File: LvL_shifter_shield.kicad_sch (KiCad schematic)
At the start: 11 parts, among them J1 Power, J2 Conn_02x08_Counter_Clockwise, J3 Conn_01x15_Socket, J4 Conn_01x15_Socket, U1 TXB0108DQSR, U2 TXB0108DQSR

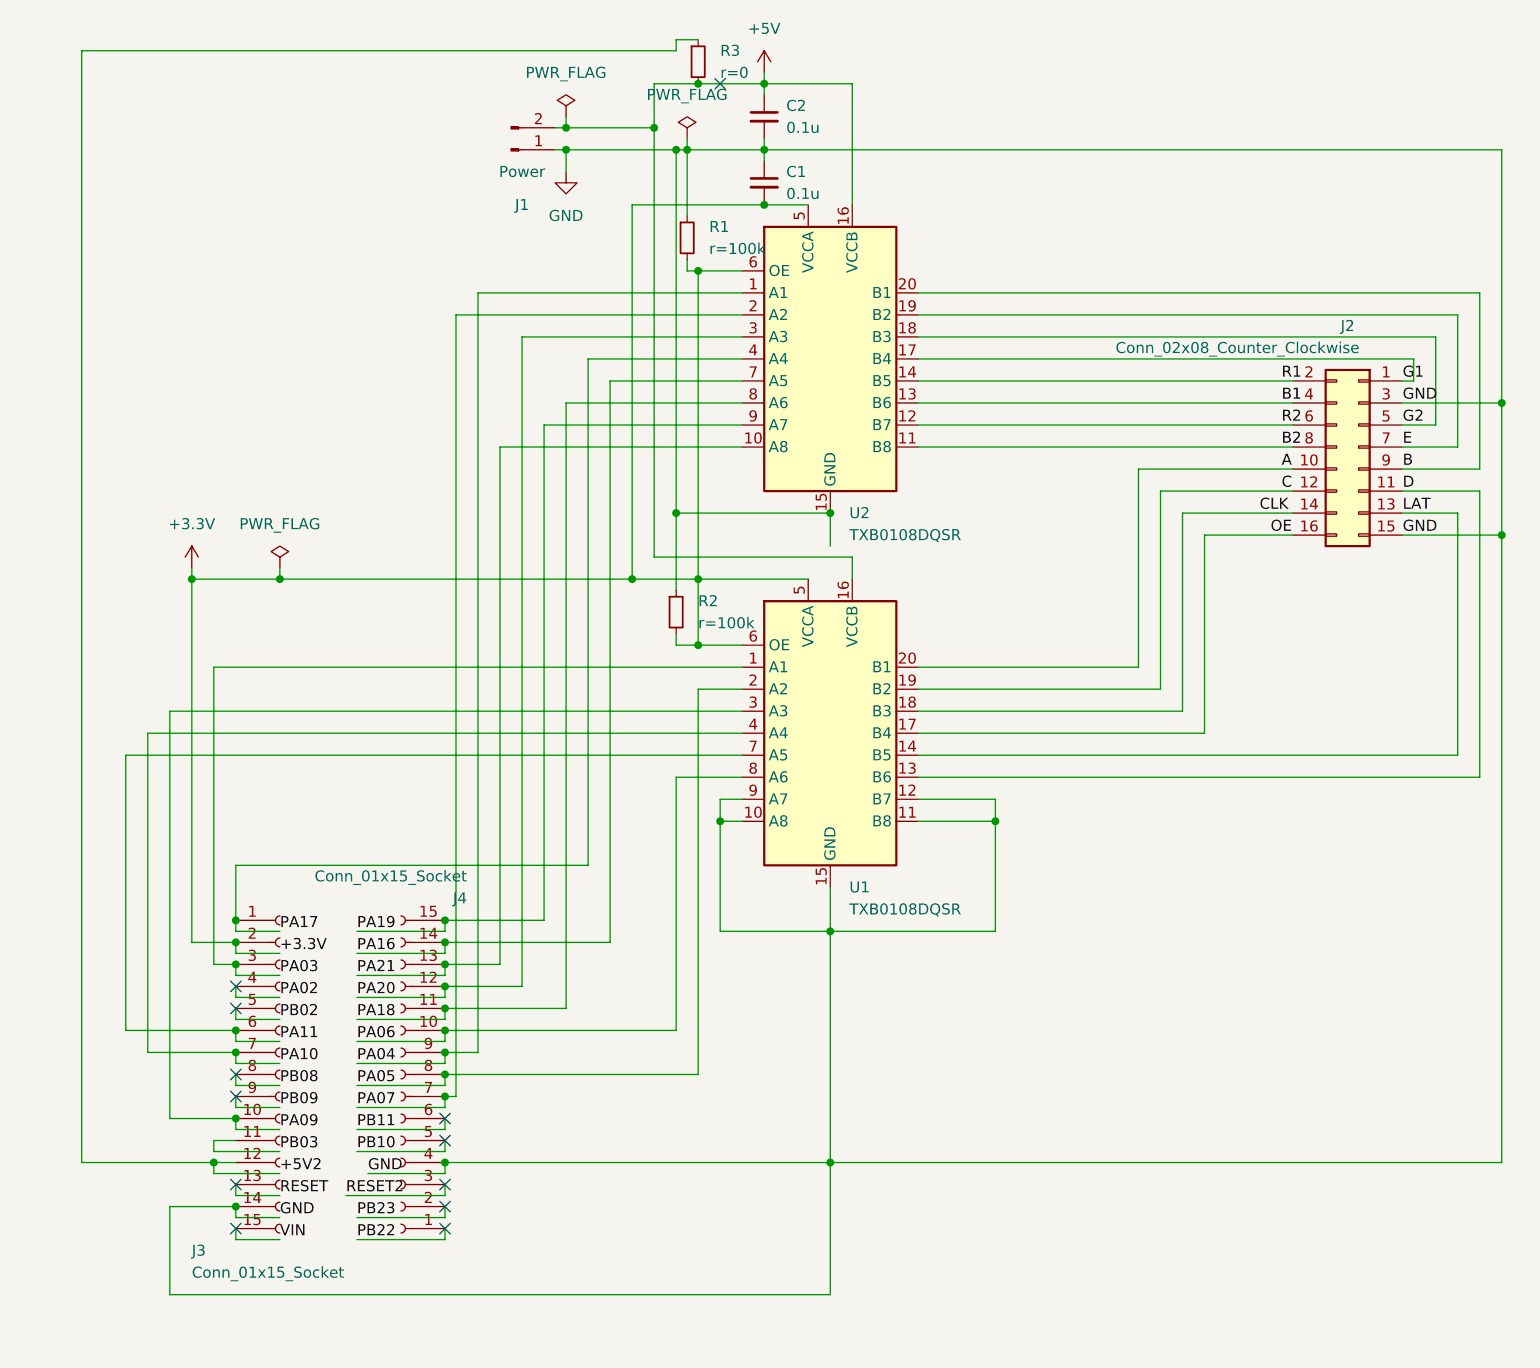
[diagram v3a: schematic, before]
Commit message: switched pin PA03 and PA02, added internal 5V
the dip switch can be used to get external 5v, internal or when none is selected the usb 5v from the arduino
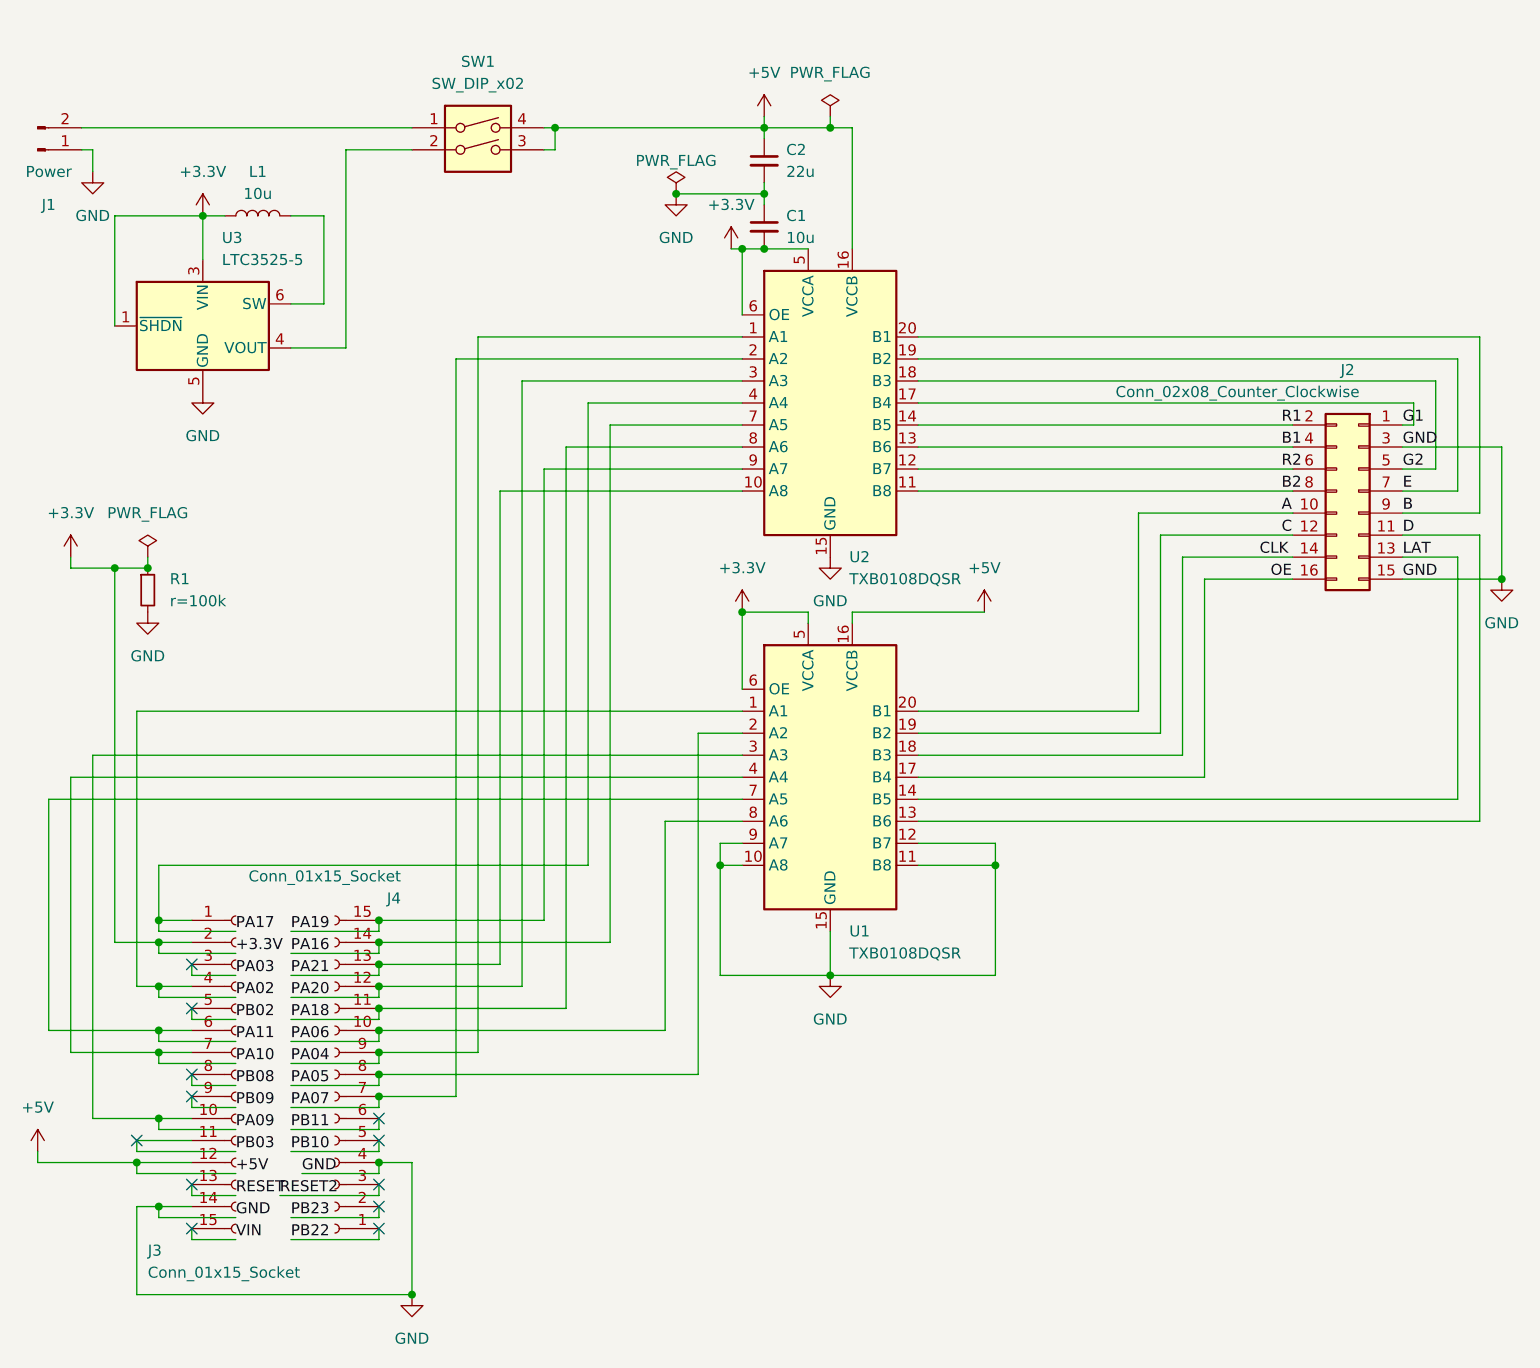
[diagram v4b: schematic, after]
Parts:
- removed R2: r=100k, Resistor_SMD:R_1206_3216Metric_Pad1.30x1.75mm_HandSolder, symbol Device:R_Small
- removed R3: r=0, Resistor_SMD:R_0603_1608Metric_Pad0.98x0.95mm_HandSolder, symbol Device:R_Small
- added L1: 10u, Inductor_SMD:L_1008_2520Metric_Pad1.43x2.20mm_HandSolder, symbol Device:L
- added SW1: SW_DIP_x02, Button_Switch_SMD:SW_DIP_SPSTx02_Slide_Copal_CHS-02A_W5.08mm_P1.27mm_JPin, symbol Switch:SW_DIP_x02
- added U3: LTC3525-5, Package_TO_SOT_SMD:SOT-363_SC-70-6, symbol Regulator_Switching:LTC3525-5
- C1: value 0.1u -> 10u
- C2: value 0.1u -> 22u
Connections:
- net +5V2 is gone; now on net +5V: J3.12 (Pin_12)
- net +3.3V: now also R1.1, L1.1, U3.1 (~{SHDN}), U3.3 (VIN); no longer R1.2
- net +5V: now also SW1.3, SW1.4; no longer J1.2 (Pin_2)
- net GND: now also R1.2, U3.2 (GND), U3.5 (GND); no longer R1.1
- net PA02: now also U1.1 (A1)
- net PA03: no longer U1.1 (A1)
- new net: J1.2 (Pin_2), SW1.1
- new net: SW1.2, U3.4 (VOUT)
- new net: L1.2, U3.6 (SW)
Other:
- moved on the sheet: C1, C2, J1, J2, J3, J4, R1, U1, U2
